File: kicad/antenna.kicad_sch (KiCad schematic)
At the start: 8 parts, among them J7 Conn_Coaxial_Small, J8 Conn_Coaxial_Small, J9 Conn_Coaxial_Small

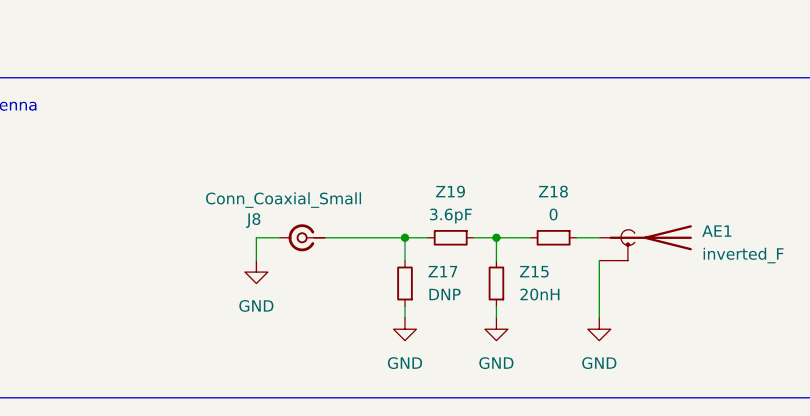
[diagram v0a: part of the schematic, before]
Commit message: files ready for production, but with wrong stackup (3313)
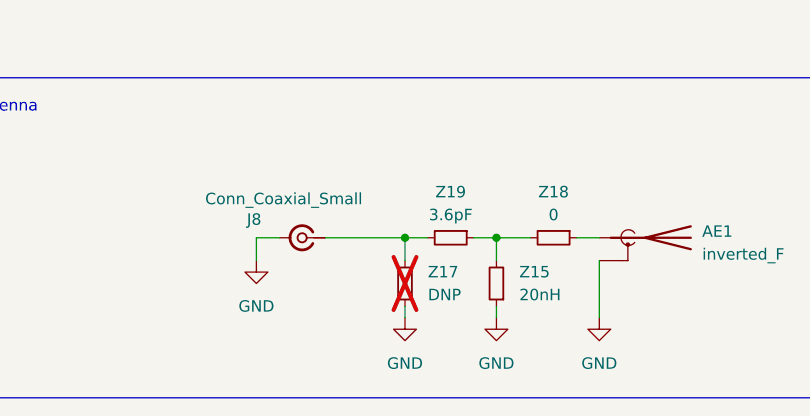
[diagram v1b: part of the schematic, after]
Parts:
- Z17: now not fitted
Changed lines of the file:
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@@
 		(in_bom yes)
 		(on_board yes)
-		(dnp no)
+		(dnp yes)
 		(fields_autoplaced yes)
 		(property "Reference" "Z17"

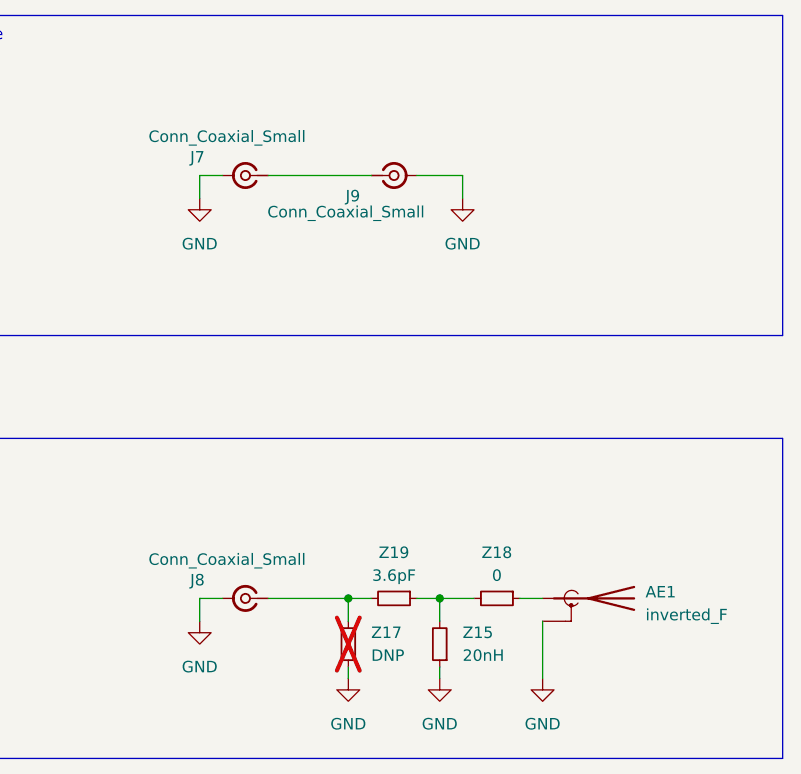
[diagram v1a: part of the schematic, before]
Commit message: [kicad] Update to kicad 9
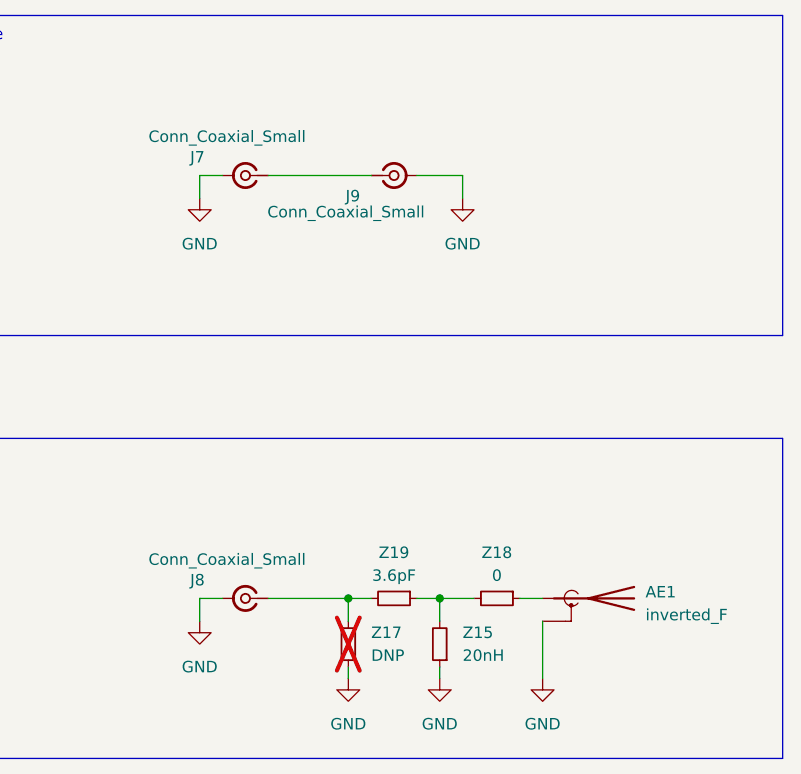
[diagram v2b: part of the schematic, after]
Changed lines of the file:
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@@
 (kicad_sch
-	(version 20231120)
+	(version 20250114)
 	(generator "eeschema")
-	(generator_version "8.0")
+	(generator_version "9.0")
 	(paper "A4")
+	(rectangle
+		(start 90.17 93.98)
+		(end 187.96 129.54)
+		(stroke
+			(width 0)
+			(type default)
+		)
+		(fill
+			(type none)
+		)
+	)
+	(rectangle
+		(start 90.17 46.99)
+		(end 187.96 82.55)
+		(stroke
+			(width 0)
+			(type default)
+		)
+		(fill
+			(type none)
+		)
+	)
+	(text "Antenna"
+		(exclude_from_sim no)
+		(at 95.25 97.282 0)
+		(effects
+			(font
+				(size 1.27 1.27)
+			)
+		)
+	)
+	(text "Impedance"
+		(exclude_from_sim no)
+		(at 96.52 49.276 0)
+		(effects
+			(font
+				(size 1.27 1.27)
+			)
+		)
+	)
+	(text "Antenna Notes:\n- LoRaWan\n	- 868 MHz (EU)\n	- 915 MHz (AM)\n- GNSS (GPS) Frequency is \n	- For L1: 1575.42\n	- For L2: 1227.6\n	- For L5: 1176.45\n- The stackup for the first 3 layers\n	- 0.035 mm (Cu)\n	- 0.2104 mm (Prepreg - 7628*1)\n	- 0.0152 mm (Cu)\nLink: https://jlcpcb.com/impedance"
+		(exclude_from_sim no)
+		(at 21.082 74.93 0)
+		(effects
+			(font
+				(size 1.27 1.27)
+			)
+			(justify left)
+		)
+	)
+	(text "Notes:\n- The dielectric constant is 4.4\n- The stackup for the first 3 layers\n	- 0.035 mm (Cu)\n	- 0.2104 mm (Prepreg - 7628*1)\n	- 0.0152 mm (Cu)\nLink: https://jlcpcb.com/impedance"
+		(exclude_from_sim no)
+		(at 18.034 32.258 0)
+		(effects
+			(font
+				(size 1.27 1.27)
+			)
+			(justify left)
+		)
+	)
 	(junction
 		(at 139.7 111.76)
@@
 		)
 	)
-	(rectangle
-		(start 90.17 93.98)
-		(end 187.96 129.54)
-		(stroke
-			(width 0)
-			(type default)
-		)
-		(fill
-			(type none)
-		)
-	)
-	(rectangle
-		(start 90.17 46.99)
-		(end 187.96 82.55)
-		(stroke
-			(width 0)
-			(type default)
-		)
-		(fill
-			(type none)
-		)
-	)
-	(text "Antenna"
-		(exclude_from_sim no)
-		(at 95.25 97.282 0)
-		(effects
-			(font
-				(size 1.27 1.27)
-			)
-		)
-	)
-	(text "Impedance"
-		(exclude_from_sim no)
-		(at 96.52 49.276 0)
-		(effects
-			(font
-				(size 1.27 1.27)
-			)
-		)
-	)
-	(text "Antenna Notes:\n- LoRaWan\n	- 868 MHz (EU)\n	- 915 MHz (AM)\n- GNSS (GPS) Frequency is \n	- For L1: 1575.42\n	- For L2: 1227.6\n	- For L5: 1176.45\n- The stackup for the first 3 layers\n	- 0.035 mm (Cu)\n	- 0.2104 mm (Prepreg - 7628*1)\n	- 0.0152 mm (Cu)\nLink: https://jlcpcb.com/impedance"
-		(exclude_from_sim no)
-		(at 21.082 74.93 0)
-		(effects
-			(font
-				(size 1.27 1.27)
-			)
-			(justify left)
-		)
-	)
-	(text "Notes:\n- The dielectric constant is 4.4\n- The stackup for the first 3 layers\n	- 0.035 mm (Cu)\n	- 0.2104 mm (Prepreg - 7628*1)\n	- 0.0152 mm (Cu)\nLink: https://jlcpcb.com/impedance"
-		(exclude_from_sim no)
-		(at 18.034 32.258 0)
-		(effects
-			(font
-				(size 1.27 1.27)
-			)
-			(justify left)
-		)
-	)
